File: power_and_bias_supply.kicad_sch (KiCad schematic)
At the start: 42 parts, among them Q501 2N7002, U501 MCP6L02x-xSN, U502 LM2733YMFX/NOPB, U503 TPS22944DCKR, X5 Conn_Coaxial

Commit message: worked on bom. some changes. added license
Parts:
- C501, C503, C504, C505, C520, C550, C553, C554, C560, C568, C569, Q501, R500, R501, R502, R503, R504, R505, R506, R507, R508, R509, R512, R516: JLC_placed_by (none) -> yes
- D500, L500, L501, U501, U503, X5: JLC_placed_by (none) -> no
- JP500, JP501, JP502, JP503, JP504, JP505, JP506, TP502, TP503, TP504, TP505: JLC_placed_by (none) -> never
- U502: JLC_placed_by (none) -> yes; JLCplace (none) -> C527399
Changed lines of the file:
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@@
+      (effects (font (size 1.27 1.27)) hide)
+    )
+    (property "JLC_placed_by" "never" (id 5) (at 120.65 38.1 0)
       (effects (font (size 1.27 1.27)) hide)
     )
@@
       (effects (font (size 1.27 1.27)) hide)
     )
+    (property "JLC_placed_by" "no" (id 9) (at 254 54.61 0)
+      (effects (font (size 1.27 1.27)) hide)
+    )
     (pin "1")
     (pin "2")
@@
       (effects (font (size 1.27 1.27)) hide)
     )
+    (property "JLC_placed_by" "yes" (id 10) (at 207.01 127 0)
+      (effects (font (size 1.27 1.27)) hide)
+    )
     (pin "1")
     (pin "2")
@@
     )
     (property "JLCType" "MCP6L02T-E/SN" (id 8) (at 177.8 144.78 0)
+      (effects (font (size 1.27 1.27)) hide)
+    )
+    (property "JLC_placed_by" "no" (id 9) (at 177.8 144.78 0)
       (effects (font (size 1.27 1.27)) hide)
     )
@@
     )
     (property "Supplier" "Mouser" (id 5) (at 46.99 72.39 0)
+      (effects (font (size 1.27 1.27)) hide)
+    )
+    (property "JLC_placed_by" "no" (id 6) (at 46.99 72.39 0)
       (effects (font (size 1.27 1.27)) hide)
     )
@@
       (effects (font (size 1.27 1.27)) hide)
     )
+    (property "JLC_placed_by" "never" (id 5) (at 64.77 41.91 0)
+      (effects (font (size 1.27 1.27)) hide)
+    )
     (pin "1")
     (pin "2")
@@
     )
     (property "JLCplace" "C17673" (id 9) (at 119.38 87.63 0)
+      (effects (font (size 1.27 1.27)) hide)
+    )
+    (property "JLC_placed_by" "yes" (id 10) (at 119.38 87.63 0)
       (effects (font (size 1.27 1.27)) hide)
     )
@@
       (effects (font (size 1.27 1.27)) hide)
     )
+    (property "JLC_placed_by" "no" (id 9) (at 222.25 87.63 0)
+      (effects (font (size 1.27 1.27)) hide)
+    )
     (pin "1")
     (pin "2")
@@
     )
     (property "JLCplace" "C26108" (id 9) (at 189.23 80.01 0)
+      (effects (font (size 1.27 1.27)) hide)
+    )
+    (property "JLC_placed_by" "yes" (id 10) (at 189.23 80.01 0)
       (effects (font (size 1.27 1.27)) hide)
     )
@@
       (effects (font (size 1.27 1.27)) hide)
     )
+    (property "JLC_placed_by" "yes" (id 10) (at 143.51 72.39 0)
+      (effects (font (size 1.27 1.27)) hide)
+    )
     (pin "1")
     (pin "2")
@@
     )
     (property "JLCplace" "C29823" (id 9) (at 104.14 147.32 0)
+      (effects (font (size 1.27 1.27)) hide)
+    )
+    (property "JLC_placed_by" "yes" (id 10) (at 104.14 147.32 0)
       (effects (font (size 1.27 1.27)) hide)
     )
@@
       (effects (font (size 1.27 1.27)) hide)
     )
+    (property "JLC_placed_by" "never" (id 5) (at 242.57 87.63 0)
+      (effects (font (size 1.27 1.27)) hide)
+    )
     (pin "1")
     (pin "2")
@@
     )
     (property "JLCplace" "C17514" (id 9) (at 189.23 95.25 0)
+      (effects (font (size 1.27 1.27)) hide)
+    )
+    (property "JLC_placed_by" "yes" (id 10) (at 189.23 95.25 0)
       (effects (font (size 1.27 1.27)) hide)
     )
@@
       (effects (font (size 1.27 1.27)) hide)
     )
+    (property "JLC_placed_by" "yes" (id 10) (at 173.99 80.01 0)
+      (effects (font (size 1.27 1.27)) hide)
+    )
     (pin "1")
     (pin "2")
@@
     )
     (property "JLCplace" "C46653" (id 9) (at 207.01 88.9 0)
+      (effects (font (size 1.27 1.27)) hide)
+    )
+    (property "JLC_placed_by" "yes" (id 10) (at 207.01 88.9 0)
       (effects (font (size 1.27 1.27)) hide)
     )
@@
       (effects (font (size 1.27 1.27)) hide)
     )
+    (property "JLC_placed_by" "no" (id 9) (at 78.74 41.91 0)
+      (effects (font (size 1.27 1.27)) hide)
+    )
     (pin "1")
     (pin "2")
@@
       (effects (font (size 1.27 1.27)) hide)
     )
+    (property "JLC_placed_by" "yes" (id 10) (at 90.17 95.25 0)
+      (effects (font (size 1.27 1.27)) hide)
+    )
     (pin "1")
     (pin "2")
@@
       (effects (font (size 1.27 1.27)) hide)
     )
+    (property "JLC_placed_by" "never" (id 5) (at 240.03 48.26 0)
+      (effects (font (size 1.27 1.27)) hide)
+    )
     (pin "1")
   )
@@
       (effects (font (size 1.27 1.27)) hide)
     )
+    (property "JLC_placed_by" "yes" (id 10) (at 147.32 85.09 0)
+      (effects (font (size 1.27 1.27)) hide)
+    )
     (pin "1")
     (pin "2")
@@
     )
     (property "JLCplace" "C28323" (id 9) (at 93.98 147.32 0)
+      (effects (font (size 1.27 1.27)) hide)
+    )
+    (property "JLC_placed_by" "yes" (id 10) (at 93.98 147.32 0)
       (effects (font (size 1.27 1.27)) hide)
     )
@@
       (effects (font (size 1.27 1.27)) hide)
     )
+    (property "JLC_placed_by" "no" (id 9) (at 222.25 125.73 0)
+      (effects (font (size 1.27 1.27)) hide)
+    )
     (pin "5")
     (pin "6")
@@
       (effects (font (size 1.27 1.27)) hide)
     )
+    (property "JLC_placed_by" "yes" (id 10) (at 21.59 91.44 0)
+      (effects (font (size 1.27 1.27)) hide)
+    )
     (pin "1")
     (pin "2")
@@
       (effects (font (size 1.27 1.27)) hide)
     )
+    (property "JLC_placed_by" "yes" (id 10) (at 173.99 95.25 0)
+      (effects (font (size 1.27 1.27)) hide)
+    )
     (pin "1")
     (pin "2")
@@
     )
     (property "JLCplace" "C29823" (id 9) (at 48.26 161.29 0)
+      (effects (font (size 1.27 1.27)) hide)
+    )
+    (property "JLC_placed_by" "yes" (id 10) (at 48.26 161.29 0)
       (effects (font (size 1.27 1.27)) hide)
     )
@@
       (effects (font (size 1.27 1.27)) hide)
     )
+    (property "JLC_placed_by" "no" (id 9) (at 71.12 72.39 0)
+      (effects (font (size 1.27 1.27)) hide)
+    )
     (pin "1")
     (pin "2")
@@
       (effects (font (size 1.27 1.27)) hide)
     )
+    (property "JLC_placed_by" "yes" (id 10) (at 152.4 91.44 0)
+      (effects (font (size 1.27 1.27)) hide)
+    )
     (pin "1")
     (pin "2")
@@
     )
     (property "JLCplace" "C1716" (id 9) (at 78.74 80.01 0)
+      (effects (font (size 1.27 1.27)) hide)
+    )
+    (property "JLC_placed_by" "yes" (id 10) (at 78.74 80.01 0)
       (effects (font (size 1.27 1.27)) hide)
     )
@@
       (effects (font (size 1.27 1.27)) hide)
     )
+    (property "JLC_placed_by" "no" (id 6) (at 129.54 72.39 0)
+      (effects (font (size 1.27 1.27)) hide)
+    )
     (pin "1")
     (pin "2")
@@
       (effects (font (size 1.27 1.27)) hide)
     )
+    (property "JLC_placed_by" "yes" (id 10) (at 78.74 95.25 0)
+      (effects (font (size 1.27 1.27)) hide)
+    )
     (pin "1")
     (pin "2")
@@
     )
     (property "JLCplace" "C29823" (id 9) (at 101.6 87.63 0)
+      (effects (font (size 1.27 1.27)) hide)
+    )
+    (property "JLC_placed_by" "yes" (id 10) (at 101.6 87.63 0)
       (effects (font (size 1.27 1.27)) hide)
     )
@@
       (effects (font (size 1.27 1.27)) hide)
     )
+    (property "JLC_placed_by" "yes" (id 10) (at 181.61 72.39 0)
+      (effects (font (size 1.27 1.27)) hide)
+    )
     (pin "1")
     (pin "2")
@@
       (effects (font (size 1.27 1.27)) hide)
     )
+    (property "JLC_placed_by" "never" (id 5) (at 58.42 148.59 0)
+      (effects (font (size 1.27 1.27)) hide)
+    )
     (pin "1")
   )
@@
     )
     (property "Supplier" "--" (id 4) (at 93.98 134.62 0)
+      (effects (font (size 1.27 1.27)) hide)
+    )
+    (property "JLC_placed_by" "never" (id 5) (at 93.98 134.62 0)
       (effects (font (size 1.27 1.27)) hide)
     )
@@
       (effects (font (size 1.27 1.27)) hide)
     )
+    (property "JLC_placed_by" "yes" (id 9) (at 46.99 85.09 0)
+      (effects (font (size 1.27 1.27)) hide)
+    )
+    (property "JLCplace" "C527399" (id 10) (at 46.99 85.09 0)
+      (effects (font (size 1.27 1.27)) hide)
+    )
     (pin "1")
     (pin "2")
@@
     )
     (property "JLCplace" "C49678" (id 9) (at 40.64 46.99 0)
+      (effects (font (size 1.27 1.27)) hide)
+    )
+    (property "JLC_placed_by" "yes" (id 10) (at 40.64 46.99 0)
       (effects (font (size 1.27 1.27)) hide)
     )
@@
       (effects (font (size 1.27 1.27)) hide)
     )
+    (property "JLC_placed_by" "never" (id 5) (at 90.17 104.14 0)
+      (effects (font (size 1.27 1.27)) hide)
+    )
     (pin "1")
     (pin "2")
@@
       (effects (font (size 1.27 1.27)) hide)
     )
+    (property "JLC_placed_by" "never" (id 5) (at 134.62 19.05 0)
+      (effects (font (size 1.27 1.27)) hide)
+    )
     (pin "1")
     (pin "2")
@@
     )
     (property "JLCplace" "C17414" (id 9) (at 110.49 36.83 0)
+      (effects (font (size 1.27 1.27)) hide)
+    )
+    (property "JLC_placed_by" "yes" (id 10) (at 110.49 36.83 0)
       (effects (font (size 1.27 1.27)) hide)
     )
@@
       (effects (font (size 1.27 1.27)) hide)
     )
+    (property "JLC_placed_by" "never" (id 5) (at 127 41.91 0)
+      (effects (font (size 1.27 1.27)) hide)
+    )
     (pin "1")
     (pin "2")
@@
       (effects (font (size 1.27 1.27)) hide)
     )
+    (property "JLC_placed_by" "never" (id 5) (at 147.32 99.06 0)
+      (effects (font (size 1.27 1.27)) hide)
+    )
     (pin "1")
     (pin "2")
@@
       (effects (font (size 1.27 1.27)) hide)
     )
+    (property "JLC_placed_by" "yes" (id 10) (at 167.64 144.78 0)
+      (effects (font (size 1.27 1.27)) hide)
+    )
     (pin "1")
     (pin "2")
@@
     )
     (property "JLCplace" "C17556" (id 9) (at 90.17 80.01 0)
+      (effects (font (size 1.27 1.27)) hide)
+    )
+    (property "JLC_placed_by" "yes" (id 10) (at 90.17 80.01 0)
       (effects (font (size 1.27 1.27)) hide)
     )
@@
     )
     (property "JLCplace" "C1710" (id 9) (at 220.98 62.23 0)
+      (effects (font (size 1.27 1.27)) hide)
+    )
+    (property "JLC_placed_by" "yes" (id 10) (at 220.98 62.23 0)
       (effects (font (size 1.27 1.27)) hide)
     )
@@
       (effects (font (size 1.27 1.27)) hide)
     )
+    (property "JLC_placed_by" "never" (id 5) (at 242.57 125.73 0)
+      (effects (font (size 1.27 1.27)) hide)
+    )

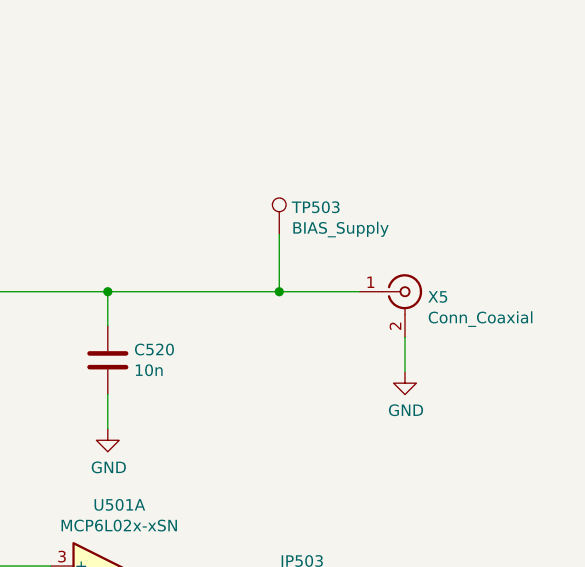
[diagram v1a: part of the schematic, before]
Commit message: Updated schematic and pcb to use global muonpi library
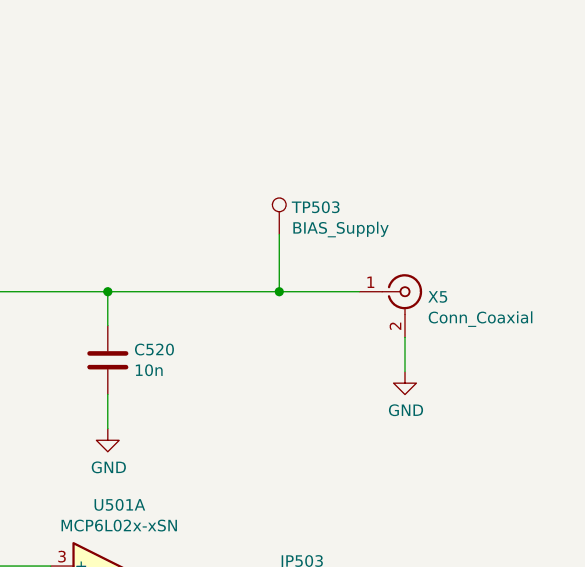
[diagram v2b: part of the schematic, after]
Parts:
- U503: symbol muonpi-kicad-library:TPS22944DCKR -> muonpi:TPS22944DCKR
- X5: footprint muonpi-kicad-library:Connector_Coaxial_SMA_edge_combined -> muonpi:SMA_Samtec_SMA-J-P-X-ST-EM1_EdgeMount; symbol Connector:Conn_Coaxial -> muonpi:Conn_Coaxial
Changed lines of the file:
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@@
     (pin "1")
   )
-  (symbol (lib_id "Connector:Conn_Coaxial") (at 254 54.61 0) (unit 1)
+  (symbol (lib_id "muonpi:Conn_Coaxial") (at 254 54.61 0) (unit 1)
     (in_bom yes) (on_board yes)
     (property "Reference" "X5" (id 0) (at 256.5401 55.2259 0)
@@
       (effects (font (size 1.27 1.27)) (justify left))
     )
-    (property "Footprint" "muonpi-kicad-library:Connector_Coaxial_SMA_edge_combined" (id 2) (at 254 54.61 0)
+    (property "Footprint" "muonpi:SMA_Samtec_SMA-J-P-X-ST-EM1_EdgeMount" (id 2) (at 254 54.61 0)
       (effects (font (size 1.27 1.27)) hide)
     )
@@
     (pin "2")
   )
-  (symbol (lib_id "muonpi-kicad-library:TPS22944DCKR") (at 78.74 41.91 0) (unit 1)
+  (symbol (lib_id "muonpi:TPS22944DCKR") (at 78.74 41.91 0) (unit 1)
     (in_bom yes) (on_board yes)
     (property "Reference" "U503" (id 0) (at 78.74 32.6198 0))
